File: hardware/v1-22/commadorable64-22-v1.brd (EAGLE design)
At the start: 33 x 40 mm, 23 parts, among them J2 SPI_TFT_DISPLAY, Q2 MOSFET-PCHANNEL, U1 NCP1117, X1 MICRO_USB_TH, X2 MICRO_USB_TH_VERTICAL, X3 ESPROGESPROG-DEVICE

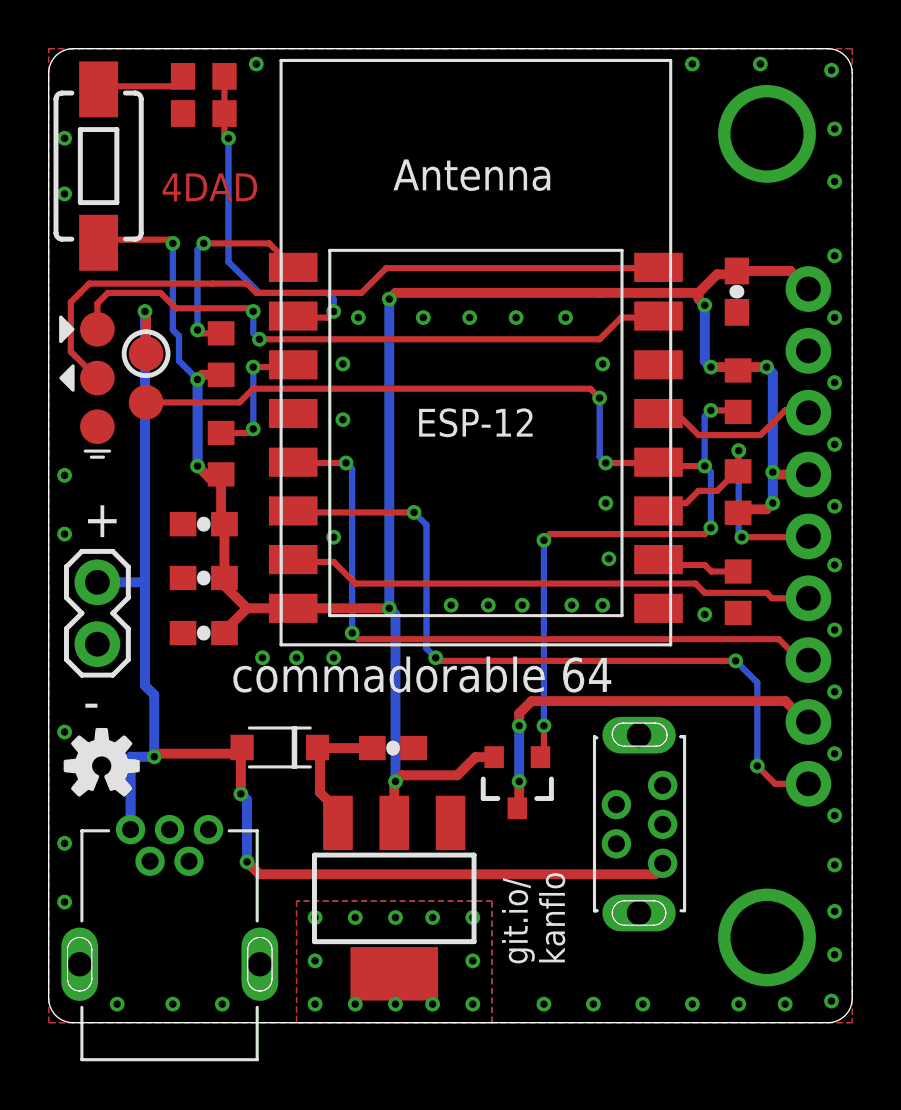
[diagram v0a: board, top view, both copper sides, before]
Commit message: Added silkscreen, separated R6, R7
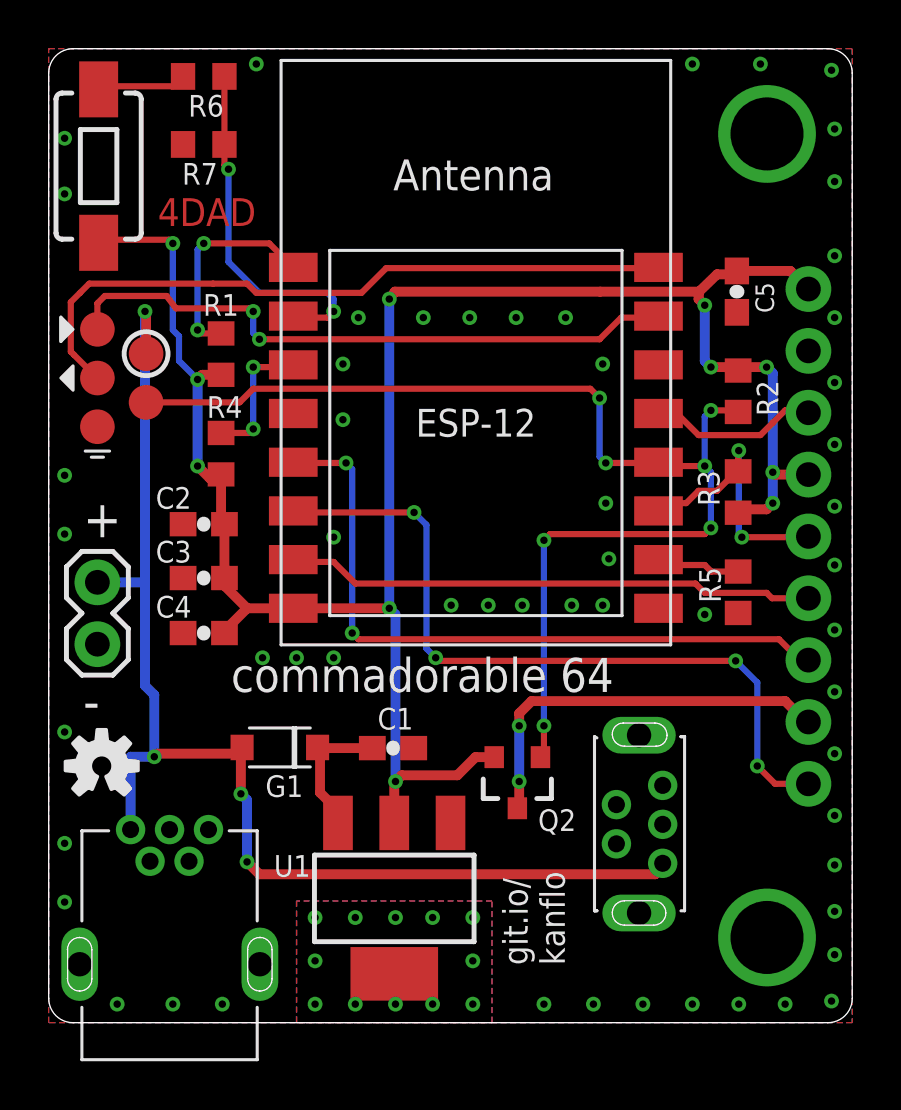
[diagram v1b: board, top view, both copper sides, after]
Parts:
- moved R7 1.27 mm to (23.4, 36.1)
